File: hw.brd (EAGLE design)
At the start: 64.8 x 81.3 mm, 37 parts, among them IC1 MIC_I2S_SPH0645, Q3 DMG3415U, U1 MAX98357A, U2 AP2112-3.3, U3 MCP73831T-2ACI/OT, X2 JSTPH

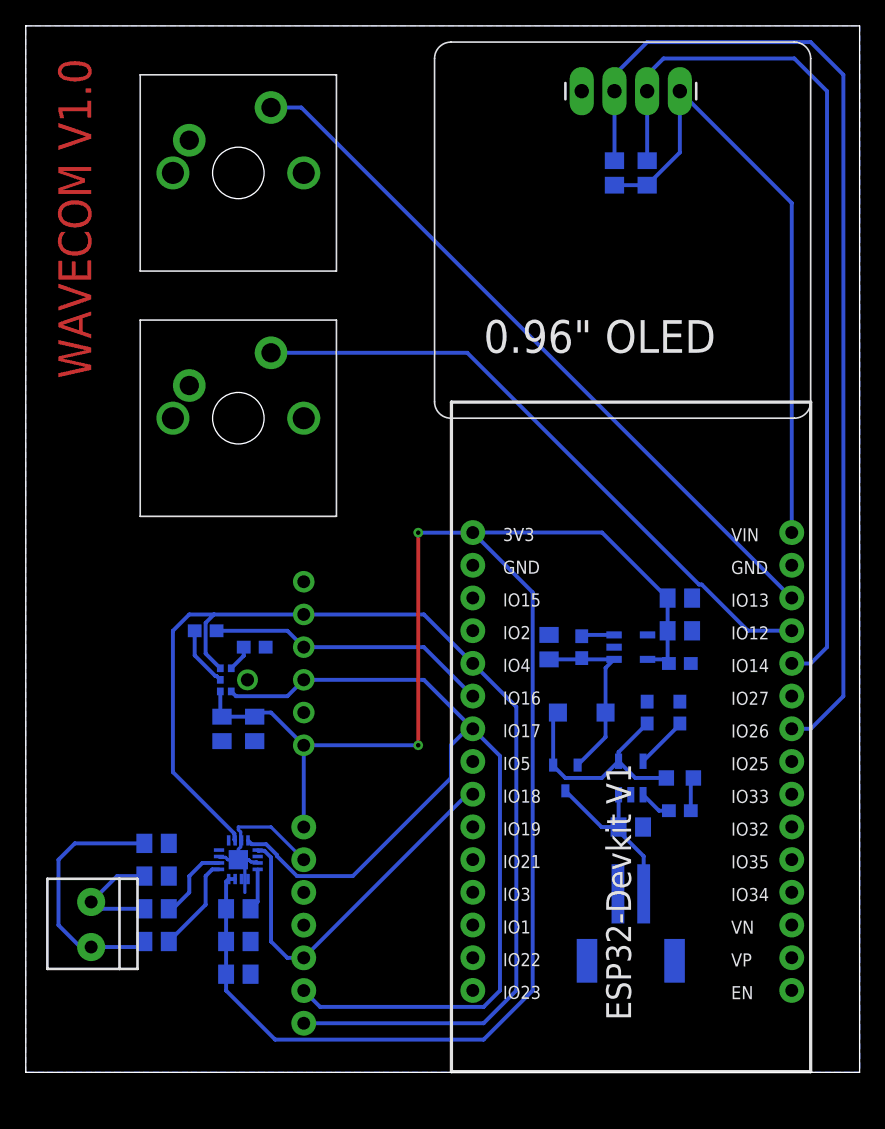
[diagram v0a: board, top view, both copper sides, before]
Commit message: flipping esp32 around
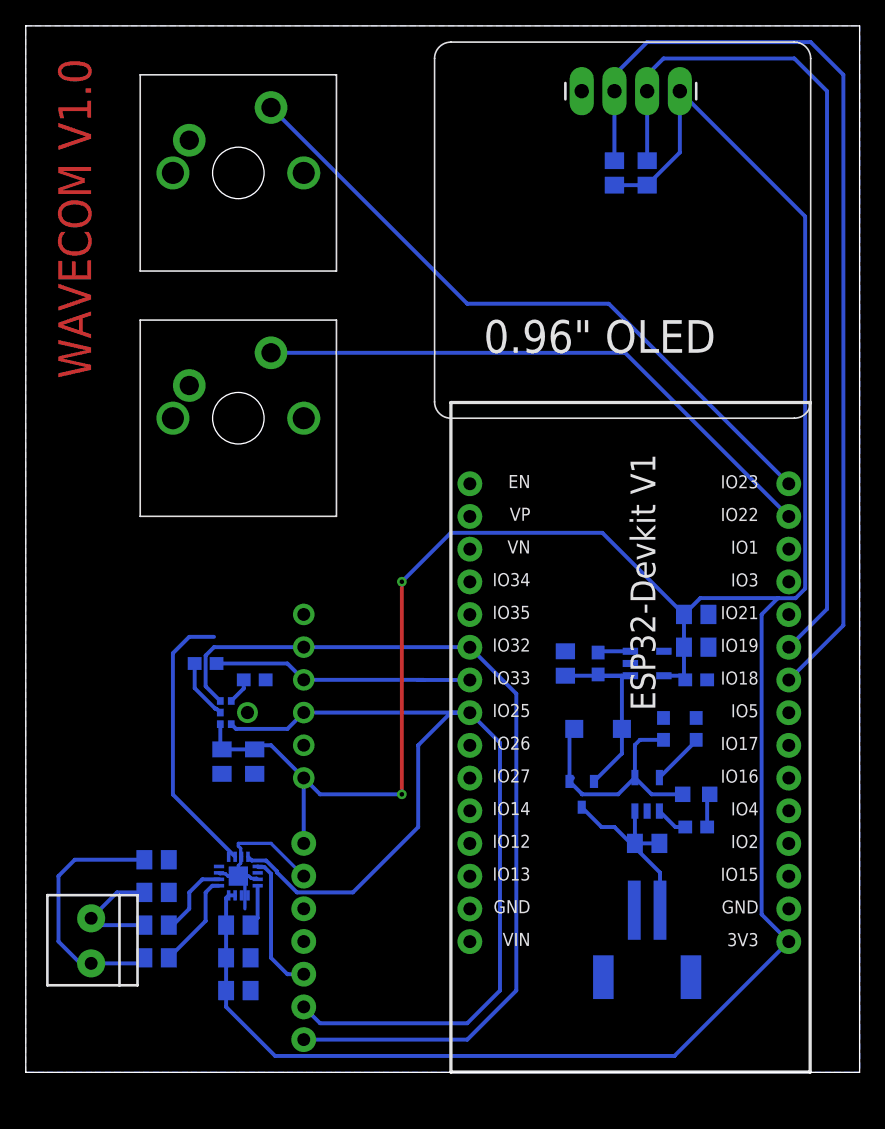
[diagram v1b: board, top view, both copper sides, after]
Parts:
- moved U$12 14.2 mm to (61.0, 33.0), turned to 90 degrees
- moved C3 2.54 mm to (30.5, 24.1)
- moved C6 2.54 mm to (33.0, 24.1)
- moved R3 2.54 mm to (33.0, 30.5)
- moved IC1 2.54 mm to (31.8, 27.9)
- moved JP2 2.54 mm to (36.8, 29.2)
- moved R2 2.54 mm to (29.2, 31.8)
- moved U2 1.80 mm to (63.5, 31.8)
- moved C10 1.80 mm to (63.5, 17.8)
- moved Q3 1.80 mm to (58.4, 21.6)
- moved U3 1.80 mm to (63.5, 21.6)
- moved X2 1.80 mm to (63.5, 8.89)
- moved C7 1.80 mm to (57.1, 31.8)
- moved R7 1.80 mm to (59.7, 31.8)
- moved C8 1.80 mm to (67.3, 30.5)
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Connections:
- net 3.3V: now also R11.2, R9.2, U$1.4
- net BCLK: now also U$12.23; no longer U$12.7
- net BTN1: now also U$12.14; no longer U$12.27
- net BTN2: now also U$12.15; no longer U$12.28
- net DIN: no longer U$12.9
- net DOUT: now also U$12.22; no longer U$12.6
- net LRCLK: now also U$12.21; no longer U$12.5
- net SCL: now also U$12.9; no longer U$12.24
- net SDA: now also U$12.10; no longer U$12.26
- net VDD: no longer R11.2, R9.2, U$1.4
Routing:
- net 3.3V: track 143.7 -> 222.7 mm
- net VDD: track 48.8 -> 0.00 mm
- net DIN: track 29.3 -> 10.9 mm
- net SCL: track 79.9 -> 75.3 mm
- net BTN1: track 49.4 -> 45.5 mm
- net BTN2: track 56.2 -> 52.3 mm
- net BCLK: track 83.4 -> 86.5 mm
- net SDA: track 68.7 -> 66.6 mm
- net VBAT: track 14.3 -> 16.2 mm
- net N$9: track 14.5 -> 16.1 mm
- net VBUS: track 18.4 -> 19.9 mm
- net DOUT: track 22.0 -> 20.6 mm

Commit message: ground planes
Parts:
- moved C3 2.54 mm to (30.5, 26.7)
- moved C6 2.54 mm to (33.0, 26.7)
- moved R3 2.54 mm to (33.0, 33.0)
- moved IC1 2.54 mm to (31.8, 30.5)
- moved JP2 2.54 mm to (36.8, 31.8)
- moved R2 2.54 mm to (29.2, 34.3)
- moved U1 1.27 mm to (31.8, 16.5)
- moved C2 1.27 mm to (31.8, 7.62)
- moved C1 1.27 mm to (31.8, 10.2)
- moved C4 1.27 mm to (25.4, 15.2)
- moved C5 1.27 mm to (25.4, 17.8)
- moved FB1 1.27 mm to (25.4, 10.2)
- moved FB2 1.27 mm to (25.4, 12.7)
- moved JP1 1.27 mm to (36.8, 11.4)
- moved R1 1.27 mm to (31.8, 12.7)
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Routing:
- net VBAT: track 16.2 -> 14.2 mm
- net LRCLK: track 92.6 -> 94.0 mm
- net VBUS: track 19.9 -> 18.5 mm
- net N$9: track 16.1 -> 14.9 mm
- net DOUT: track 20.6 -> 21.7 mm
- net GND: track 14.9 -> 15.8 mm
- net BCLK: track 86.5 -> 85.8 mm
- added copper zone on layer 1, net GND
